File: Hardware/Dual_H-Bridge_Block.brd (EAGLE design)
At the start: 30.5 x 44.5 mm, 27 parts, among them U1 TB6612FNG, U2 EDISON_CONNECTOR_FULLMOUNTING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, U3 EDISON_CONNECTOR_FULLHEADER, U4 TXB0108

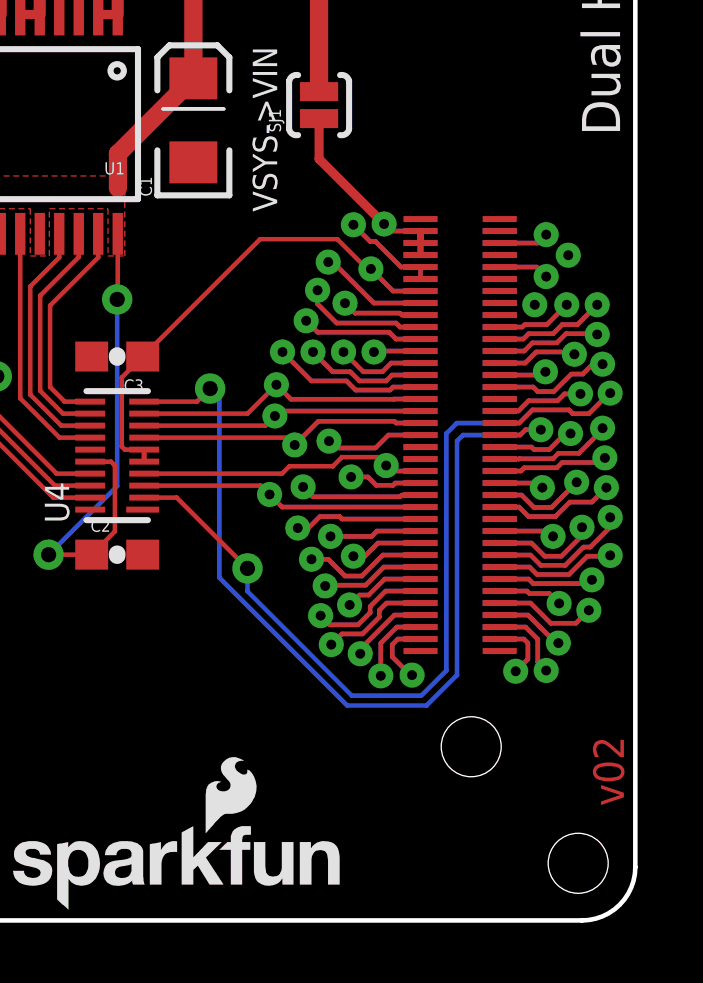
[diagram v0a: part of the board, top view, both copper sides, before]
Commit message: corrected package footprint to remove bridging.
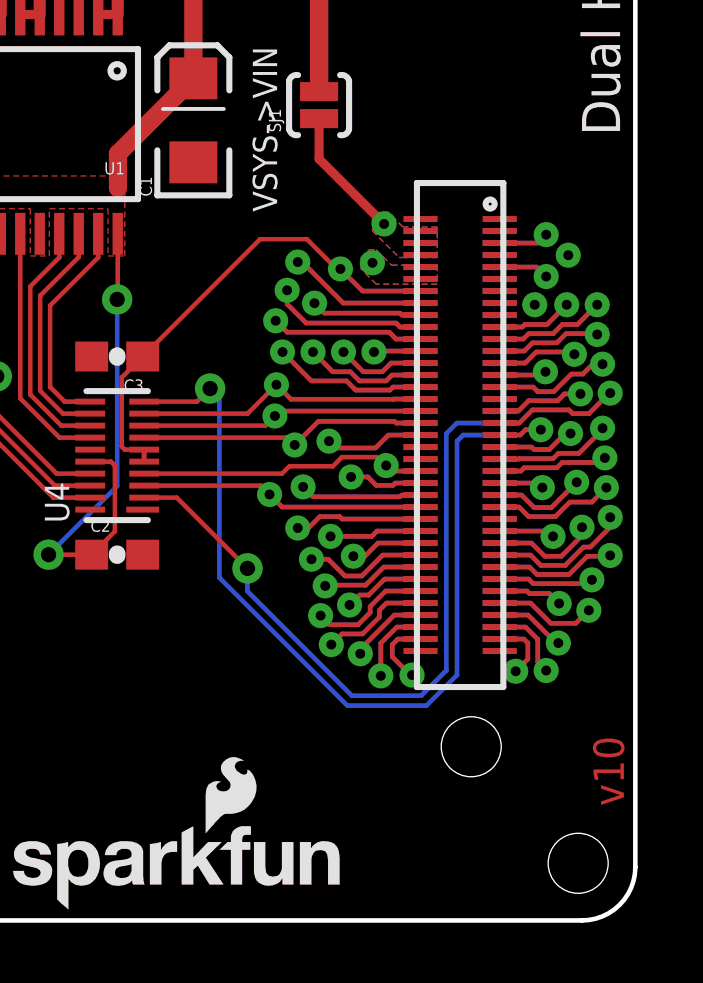
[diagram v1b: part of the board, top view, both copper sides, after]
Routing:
- net 3.3V: track 6.44 -> 0.00 mm
- net VSYS: track 9.03 -> 4.41 mm
- net USB_VBUS: track 8.13 -> 10.2 mm
- net DCIN: track 7.28 -> 9.32 mm
- net USB_DP: track 5.36 -> 7.39 mm
- net USB_DN: track 8.41 -> 10.4 mm
- net 1.8V: track 18.0 -> 19.1 mm
- added copper zone on layer 1, net 3.3V
- added copper zone on layer 16, net 3.3V
- added copper zone on layer 1, net VSYS
- added copper zone on layer 16, net VSYS
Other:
- board text added: "v10"
- board text removed: "v02"
